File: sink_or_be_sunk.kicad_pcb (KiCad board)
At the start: 2 copper layers, 117.6 x 68.7 mm, 87 parts, among them J1 Grid_Conn_LED, J10 Grid_Conn, J11 Grid_Conn, J12 Grid_Conn, J13 Grid_Conn, J14 Grid_Conn, J15 Grid_Conn, J16 Grid_Conn, J17 Mux_Conn, J18 Keypad_Conn, J19 Display_Conn, J2 Grid_Conn, J20 JTAG_Conn, J21 Debug_Conn, J22 Battery_Conn, J23 USB_B_Micro, J3 Grid_Conn, J4 Grid_Conn, J5 Grid_Conn, J6 Grid_Conn, J7 Grid_Conn, J8 Grid_Conn, J9 Grid_Conn, M1 Motor_DC, Q1 IRL530, Q2 Q_PMOS_DGS, Q3 2N3704, Q4 2N3704, SW1 SW_DPST, SW2 Reset_SW, U1 SN74HC151N, U2 LDL1117-SMD, U3 MCP73831-2-OT, U4 MCP608, U5 ESP32-WROOM-32, U6 CY7C65213A-28PVXI

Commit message: mitch-local
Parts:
- removed J17: Mux_Conn, Connector_PinHeader_2.54mm:PinHeader_1x08_P2.54mm_Vertical
- removed R1, R2, R3, R4, R5, R6, R7, R8: 20, Resistor_SMD:R_0805_2012Metric_Pad1.20x1.40mm_HandSolder
- J10, J11, J12, J13, J14, J15, J16, J9: footprint Connector_PinSocket_2.54mm:PinSocket_1x06_P2.54mm_Vertical -> Connector_PinSocket_2.54mm:PinSocket_1x02_P2.54mm_Vertical
- moved J9 287.4 mm to (113.4, 61.6), turned to 0 degrees
- moved J11 287.4 mm to (120.7, 61.6), turned to 0 degrees
- moved J10 287.3 mm to (117.1, 61.6), turned to 0 degrees
- moved J15 287.3 mm to (135.3, 61.6), turned to 0 degrees
- moved J16 287.3 mm to (139.0, 61.6), turned to 0 degrees
- moved J12 287.3 mm to (124.4, 61.6), turned to 0 degrees
- moved J14 287.3 mm to (131.7, 61.6), turned to 0 degrees
- moved J13 287.3 mm to (128.0, 61.6), turned to 0 degrees
- moved C1 286.7 mm to (189.2, 122.8)
- moved C3 286.7 mm to (138.4, 123.6)
- moved D3 286.7 mm to (203.6, 100.9)
- moved J2 286.7 mm to (105.6, 92.1)
- moved J20 286.7 mm to (100.4, 63.1)
- moved J22 286.7 mm to (201.9, 119.5)
- moved J23 286.7 mm to (203.2, 85.3)
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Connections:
- J1 pad 6: /BOAT_INPUT -> /MUX_R0
- J10 pad 2: /MUX_COL_SEL1 -> GND
- J11 pad 2: /MUX_COL_SEL1 -> GND
- J12 pad 2: /MUX_COL_SEL1 -> GND
- J13 pad 2: /MUX_COL_SEL1 -> GND
- J14 pad 2: /MUX_COL_SEL1 -> GND
- J15 pad 2: /MUX_COL_SEL1 -> GND
- J16 pad 2: /MUX_COL_SEL1 -> GND
- J2 pad 5: /BOAT_INPUT -> /MUX_R1
- J3 pad 5: /BOAT_INPUT -> /MUX_R2
- J4 pad 5: /BOAT_INPUT -> /MUX_R3
- J5 pad 5: /BOAT_INPUT -> /MUX_R4
- J6 pad 5: /BOAT_INPUT -> /MUX_R5
- J7 pad 5: /BOAT_INPUT -> /MUX_R6
- J8 pad 5: /BOAT_INPUT -> /MUX_R7
- J9 pad 2: /MUX_COL_SEL1 -> GND
- U1 pad 1: /MUX_ROW3 -> /MUX_R3
- U1 pad 12: /MUX_ROW7 -> /MUX_R7
- U1 pad 13: /MUX_ROW6 -> /MUX_R6
- U1 pad 14: /MUX_ROW5 -> /MUX_R5
- U1 pad 15: /MUX_ROW4 -> /MUX_R4
- U1 pad 2: /MUX_ROW2 -> /MUX_R2
- U1 pad 3: /MUX_ROW1 -> /MUX_R1
- U1 pad 4: /MUX_ROW0 -> /MUX_R0
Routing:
- net /BOAT_INPUT: track 110.5 -> 15.2 mm
- net /MUX_R7: track 0.00 -> 69.3 mm
- net /MUX_R6: track 0.00 -> 62.7 mm
- net /MUX_R5: track 0.00 -> 56.1 mm
- net /MUX_R4: track 0.00 -> 49.5 mm
- net /MUX_COL_SEL0: track 107.5 -> 65.0 mm
- net /MUX_COL_SEL2: track 101.2 -> 61.6 mm
- net /MUX_COL_SEL1: track 96.0 -> 58.4 mm
- net /MUX_R3: track 0.00 -> 28.0 mm, vias 0 -> 1
- net /MUX_R2: track 0.00 -> 23.8 mm, vias 0 -> 1
- net /MUX_ROW7: track 19.4 -> 0.00 mm
- net /MUX_ROW6: track 19.3 -> 0.00 mm
- net /MUX_ROW5: track 19.2 -> 0.00 mm
- net /MUX_ROW4: track 19.0 -> 0.00 mm
- net /MUX_R1: track 0.00 -> 18.4 mm
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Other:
- board size 117.6 x 68.7 mm -> 118.3 x 68.7 mm

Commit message: left off shrinking width
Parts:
- C2: value 1uF -> 4.7uF
- J1: footprint Connector_PinSocket_2.54mm:PinSocket_1x07_P2.54mm_Vertical -> Connector_JST:JST_EH_B7B-EH-A_1x07_P2.50mm_Vertical
- J10, J11, J12, J13, J14, J15, J16, J9: footprint Connector_PinSocket_2.54mm:PinSocket_1x02_P2.54mm_Vertical -> Connector_JST:JST_EH_B2B-EH-A_1x02_P2.50mm_Vertical
- J18: footprint Connector_PinSocket_2.54mm:PinSocket_1x08_P2.54mm_Vertical -> Connector_JST:JST_EH_B8B-EH-A_1x08_P2.50mm_Vertical
- J19: footprint Connector_PinHeader_2.54mm:PinHeader_1x05_P2.54mm_Vertical -> Connector_JST:JST_EH_B5B-EH-A_1x05_P2.50mm_Vertical
- J2, J3, J4, J5, J6, J7, J8: footprint Connector_PinSocket_2.54mm:PinSocket_1x06_P2.54mm_Vertical -> Connector_JST:JST_EH_B6B-EH-A_1x06_P2.50mm_Vertical
- LS1, M1: footprint Connector_PinHeader_2.54mm:PinHeader_1x02_P2.54mm_Vertical -> Connector_JST:JST_EH_B2B-EH-A_1x02_P2.50mm_Vertical
- U2: value LDL1117-SMD -> TSR_1-2433; footprint Package_TO_SOT_SMD:SOT-223 -> Converter_DCDC:Converter_DCDC_TRACO_TSR-1_THT
- moved J3 75.0 mm to (30.9, 81.8)
- moved J2 73.5 mm to (38.0, 63.2)
- moved J1 63.8 mm to (63.9, 49.7)
- moved J4 63.5 mm to (48.3, 112.0)
- moved J5 55.4 mm to (50.6, 87.9)
- moved J6 53.5 mm to (53.5, 65.1)
- moved J7 38.9 mm to (71.1, 91.8)
- moved C2 34.1 mm to (161.6, 125.6), turned to 90 degrees
- moved J8 30.0 mm to (75.6, 69.2)
- moved C1 21.1 mm to (168.1, 123.1)
- moved D2 20.1 mm to (166.7, 88.5), turned to 90 degrees
- moved U2 17.3 mm to (176.7, 123.8)
- moved C6 15.2 mm to (184.2, 83.6), turned to 90 degrees
- moved J16 13.9 mm to (149.3, 52.3), turned to 270 degrees
- moved SW1 13.1 mm to (191.2, 106.6)
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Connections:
- U2 pad 1: GND -> /Vin
- U2 pad 2: +3V3 -> GND
- U2 pad 3: /Vin -> +3V3
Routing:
- net VBUS: track 171.0 -> 140.4 mm
- net Net-(RV1-Pad1): track 30.2 -> 7.62 mm
- net Net-(C6-Pad1): track 6.58 -> 28.8 mm
- net /SPEAKER: track 79.7 -> 65.4 mm, vias 4 -> 3
- net /Vin: track 32.9 -> 18.7 mm
- net Net-(J23-Pad3): track 40.9 -> 27.8 mm
- net +BATT: track 55.6 -> 42.5 mm, vias 1 -> 2
- net Net-(J23-Pad2): track 41.9 -> 29.0 mm
- net Net-(R24-Pad2): track 48.8 -> 36.0 mm
- net GND: track 106.6 -> 97.9 mm, vias 3 -> 5
- net /MOTOR: track 76.6 -> 68.7 mm
- net +3V3: track 182.4 -> 176.9 mm, vias 4 -> 7
- net Net-(C6-Pad2): track 10.6 -> 15.3 mm
- net Net-(D2-Pad2): track 23.6 -> 27.3 mm
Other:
- board size 118.3 x 68.7 mm -> 105 x 78.9 mm

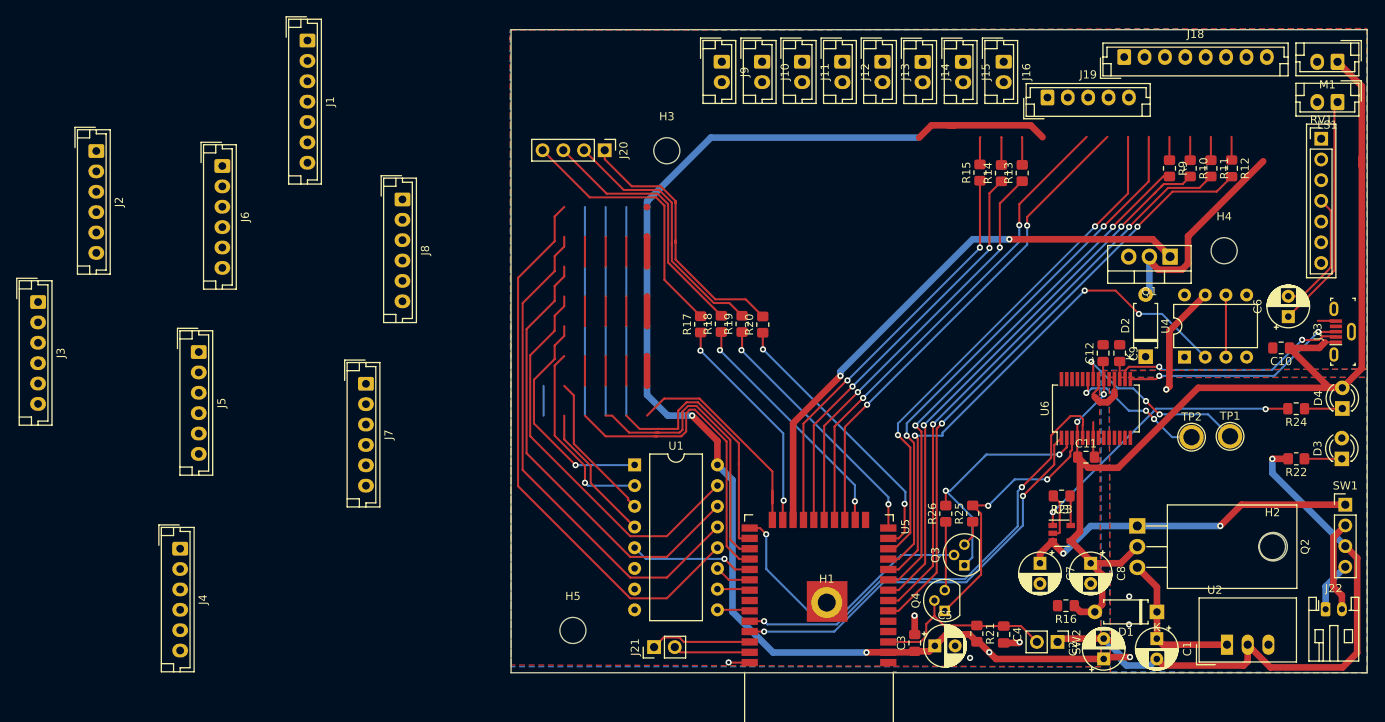
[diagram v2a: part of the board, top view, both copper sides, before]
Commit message: finsihed 79x85mm layout
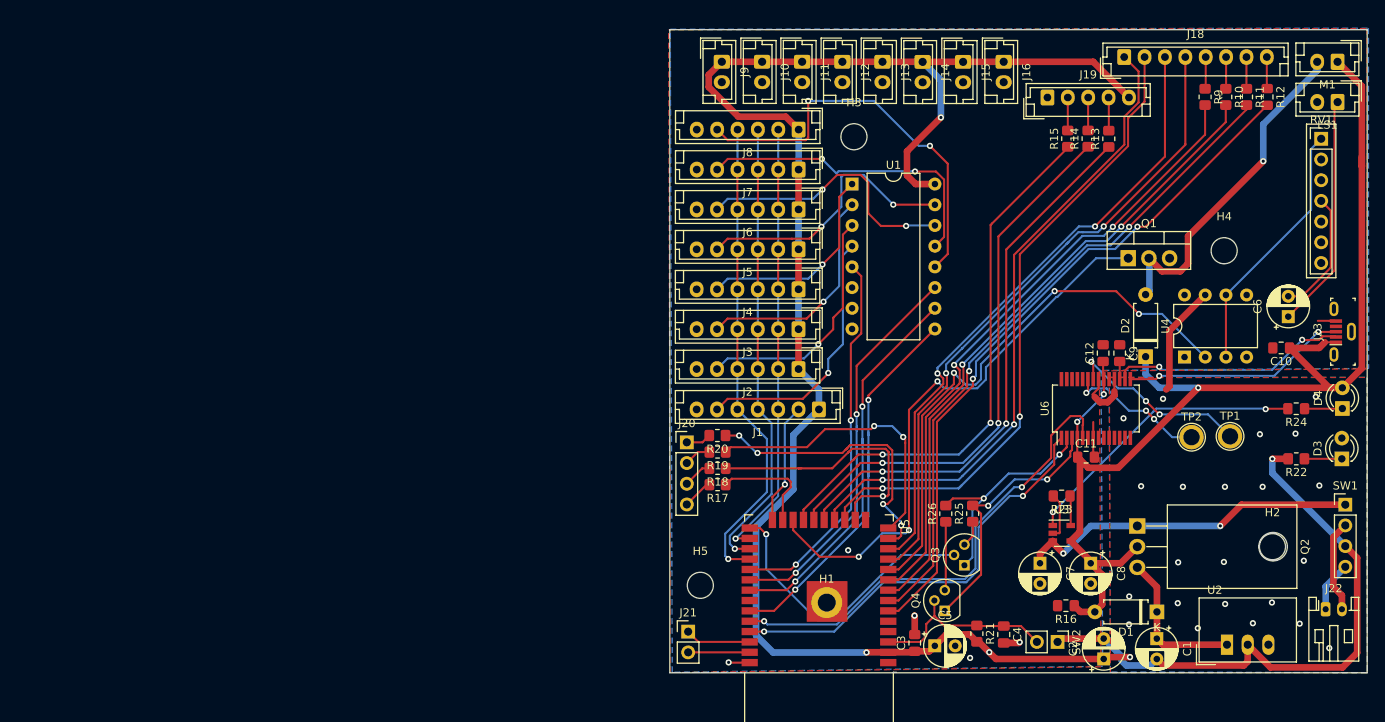
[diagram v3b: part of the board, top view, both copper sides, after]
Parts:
- moved J3 93.4 mm to (124.2, 85.1), turned to 180 degrees
- moved J2 90.2 mm to (124.2, 90.0), turned to 180 degrees
- moved J4 82.3 mm to (124.2, 80.2), turned to 180 degrees
- moved J1 77.4 mm to (126.7, 95.0), turned to 180 degrees
- moved J5 74.7 mm to (124.2, 75.3), turned to 180 degrees
- moved J6 70.9 mm to (124.2, 70.4), turned to 180 degrees
- moved J7 59.2 mm to (124.2, 65.5), turned to 180 degrees
- moved J8 49.4 mm to (124.2, 60.6), turned to 180 degrees
- moved U1 43.6 mm to (130.7, 67.3)
- moved J20 37.2 mm to (110.5, 99.0), turned to 0 degrees
- moved H3 23.0 mm to (131.0, 61.5)
- moved R17 19.8 mm to (114.2, 104.2), turned to 180 degrees
- moved R18 17.7 mm to (114.2, 102.2), turned to 180 degrees
- moved H5 16.6 mm to (112.1, 116.5)
- moved R19 16.0 mm to (114.2, 100.2), turned to 180 degrees
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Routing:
- net /MUX_ROW_SEL2: track 4.01 -> 49.2 mm, vias 0 -> 2
- net /MUX_ROW_SEL0: track 4.54 -> 48.9 mm, vias 0 -> 2
- net /MUX_ROW_SEL1: track 4.26 -> 47.3 mm, vias 0 -> 2
- net +3V3: track 176.9 -> 218.2 mm, vias 7 -> 26
- net /BOAT_INPUT: track 15.2 -> 46.5 mm, vias 1 -> 2
- net Net-(J20-Pad1): track 33.2 -> 3.10 mm
- net Net-(J20-Pad4): track 33.2 -> 3.78 mm
- net Net-(J20-Pad2): track 32.4 -> 3.33 mm
- net Net-(J20-Pad3): track 32.0 -> 3.55 mm
- net /MUX_R6: track 62.7 -> 38.3 mm, vias 0 -> 2
- net Net-(RV1-Pad1): track 7.62 -> 31.6 mm
- net /MUX_R5: track 56.1 -> 33.4 mm, vias 0 -> 2
- net /KEYPAD_COL0: track 59.8 -> 79.9 mm
- net /MUX_R7: track 69.3 -> 50.0 mm, vias 0 -> 2
- net /KEYPAD_COL1: track 60.3 -> 79.3 mm
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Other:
- board size 105 x 78.9 mm -> 85.6 x 78.9 mm

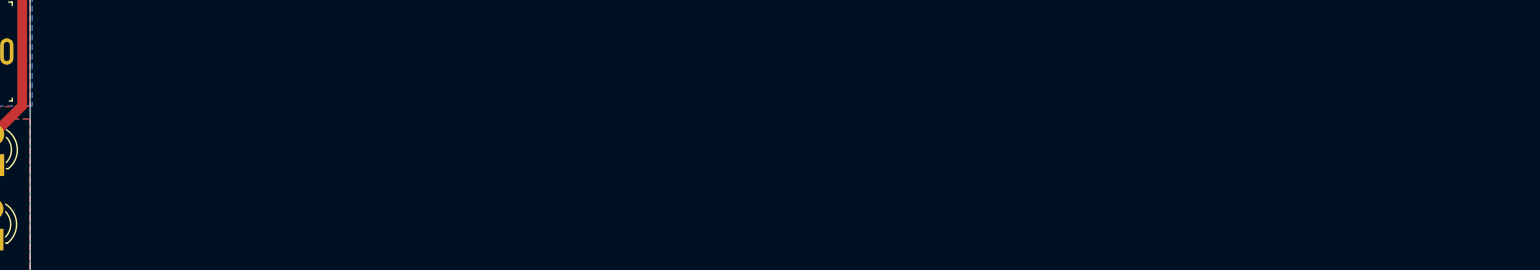
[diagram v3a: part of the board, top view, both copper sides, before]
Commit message: added some notes/questions to sch/pcb
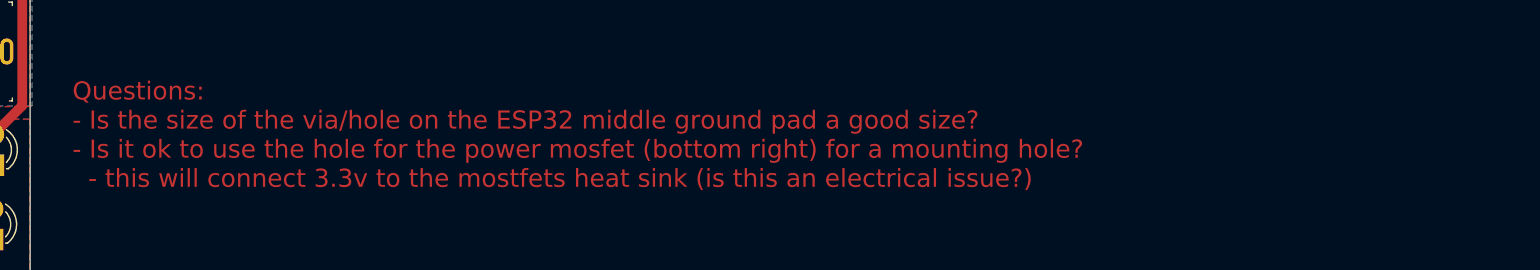
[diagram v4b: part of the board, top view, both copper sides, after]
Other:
- board text added: "Questions: - Is the size of the via/hole on the ESP32 middle ground pad a good size? - Is it ok to use the hole for the power mosfet (bottom right) for a mounting hole? - this will connect 3.3v to the mostfets heat sink (is this an electrical issue?)"

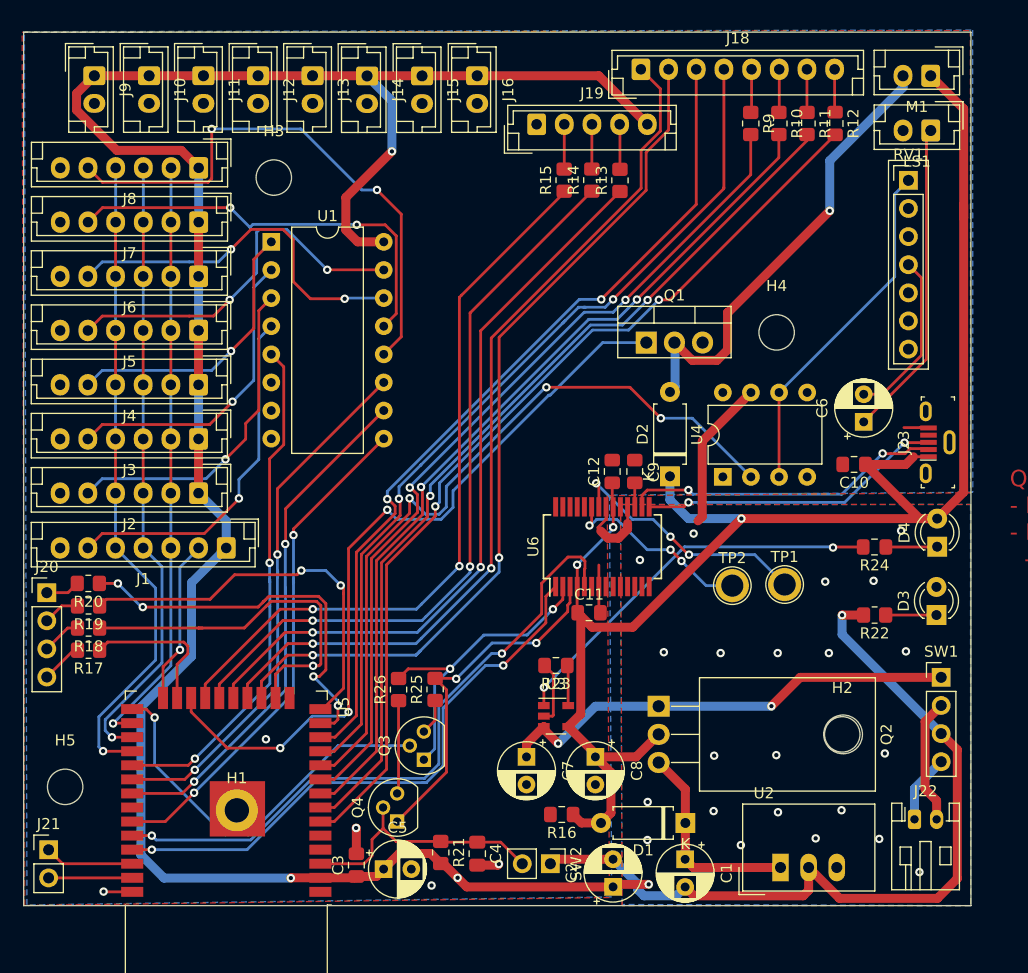
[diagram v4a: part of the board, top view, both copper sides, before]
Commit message: added new switching regulator footprint
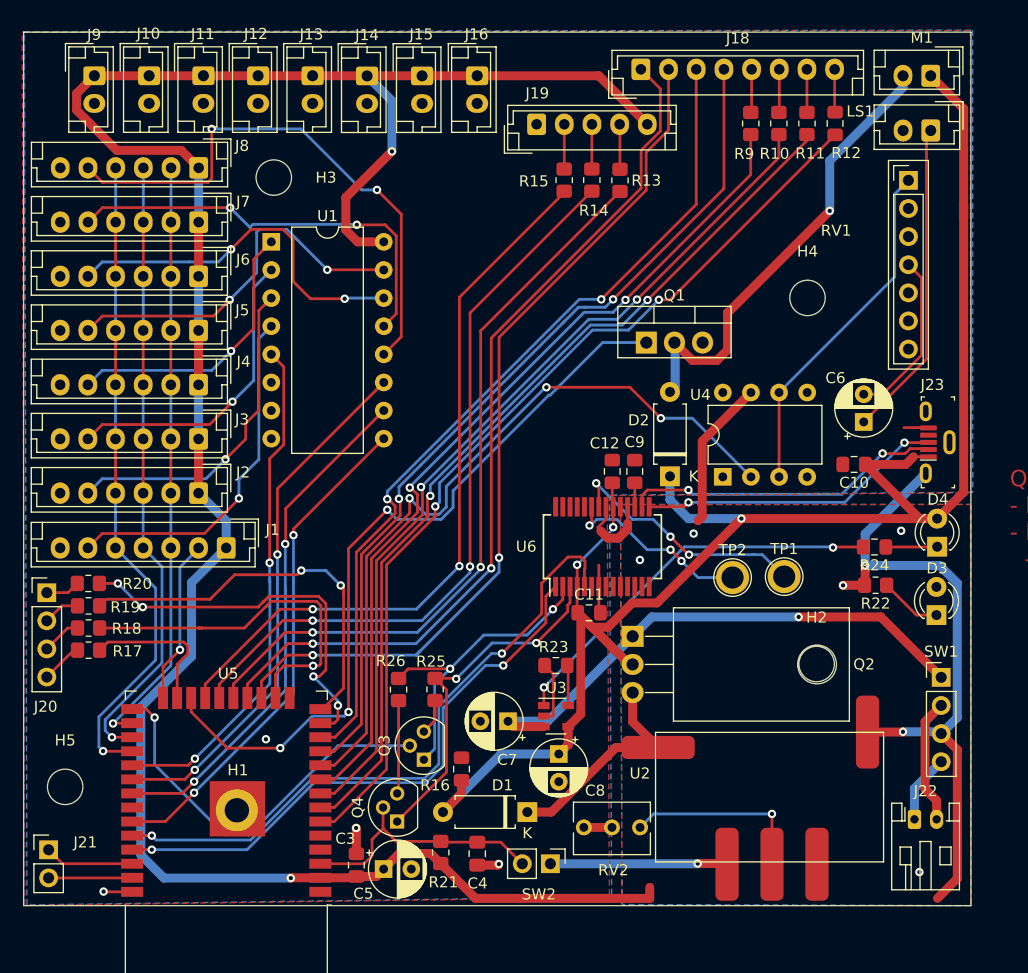
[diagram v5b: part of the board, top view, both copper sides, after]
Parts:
- removed C1, C2: 4.7uF, Capacitor_THT:CP_Radial_D5.0mm_P2.50mm
- added RV2: R_Trim (10k), Potentiometer_THT:Potentiometer_Bourns_3266Y_Vertical, F.Cu at (164.0, 120.2)
- U2: value TSR_1-2433 -> SwitchingRegulator; footprint Converter_DCDC:Converter_DCDC_TRACO_TSR-1_THT -> PCB_ESP32:SwitchingRegulator
- moved D1 14.3 mm to (153.9, 118.8)
- moved R16 9.94 mm to (147.9, 114.9), turned to 90 degrees
- moved H2 6.76 mm to (180.0, 105.4)
- moved Q2 6.74 mm to (163.4, 102.9)
- moved U2 6.26 mm to (175.5, 117.7), turned to 180 degrees
- moved H4 4.18 mm to (179.2, 72.4)
- moved C7 3.62 mm to (152.1, 110.6), turned to 180 degrees
- moved C8 3.31 mm to (156.7, 113.6)
- moved R22 2.69 mm to (185.3, 98.3)
- moved TP2 0.73 mm to (172.4, 97.6)
- moved TP1 0.72 mm to (177.1, 97.5)
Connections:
- U2 pad 3: +3V3 -> GND
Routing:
- net Net-(RV2-Pad1): track 0.00 -> 17.0 mm, vias 0 -> 1
- net +BATT: track 42.5 -> 48.7 mm, vias 2 -> 1
- net GND: track 94.2 -> 99.8 mm, vias 6 -> 8
- net VBUS: track 149.7 -> 154.2 mm
- net +3V3: track 218.2 -> 219.8 mm, vias 26 -> 6
- net /Vin: track 18.7 -> 20.2 mm
- net Net-(D3-Pad1): track 4.59 -> 5.61 mm
